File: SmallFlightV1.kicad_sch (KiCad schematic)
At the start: 0 parts

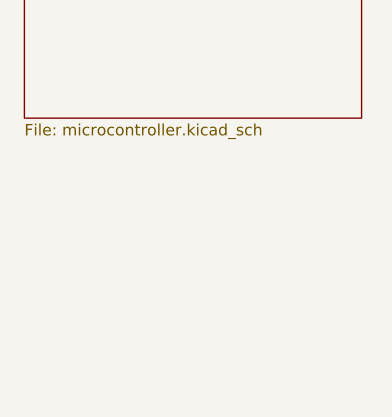
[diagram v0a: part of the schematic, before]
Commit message: more boilerplate for stm. and also power supply using LDO and USB
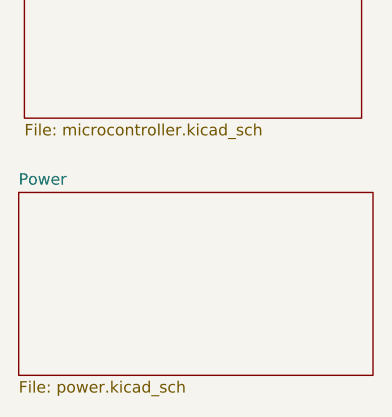
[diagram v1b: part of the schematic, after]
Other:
- added sheet Power (power.kicad_sch)
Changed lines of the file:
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@@
+		)
+	)
+	(sheet
+		(at 125.095 71.755)
+		(size 39.37 20.32)
+		(exclude_from_sim no)
+		(in_bom yes)
+		(on_board yes)
+		(dnp no)
+		(fields_autoplaced yes)
+		(stroke
+			(width 0.1524)
+			(type solid)
+		)
+		(fill
+			(color 0 0 0 0.0000)
+		)
+		(property "Sheetname" "Power"
+			(at 125.095 71.0434 0)
+			(effects
+				(font
+					(size 1.27 1.27)
+				)
+				(justify left bottom)
+			)
+		)
+		(property "Sheetfile" "power.kicad_sch"
+			(at 125.095 92.6596 0)
+			(effects
+				(font
+					(size 1.27 1.27)
+				)
+				(justify left top)
+			)
+		)
+		(instances
+			(project "SmallFlightV1"
+				(path "/5a8b04a1-a6d6-48bd-ac5f-d4986cb92d03"
+					(page "3")
+				)
+			)
 		)
 	)

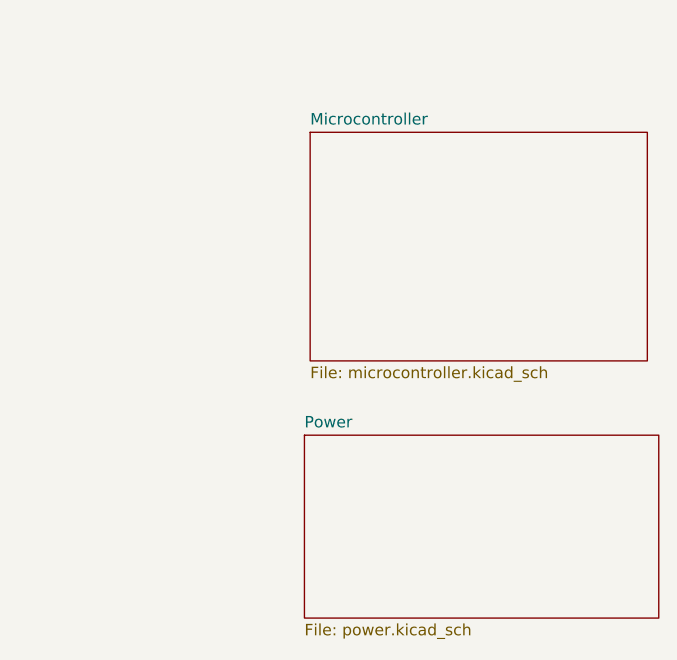
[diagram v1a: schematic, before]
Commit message: base mcu decoupling cap routing
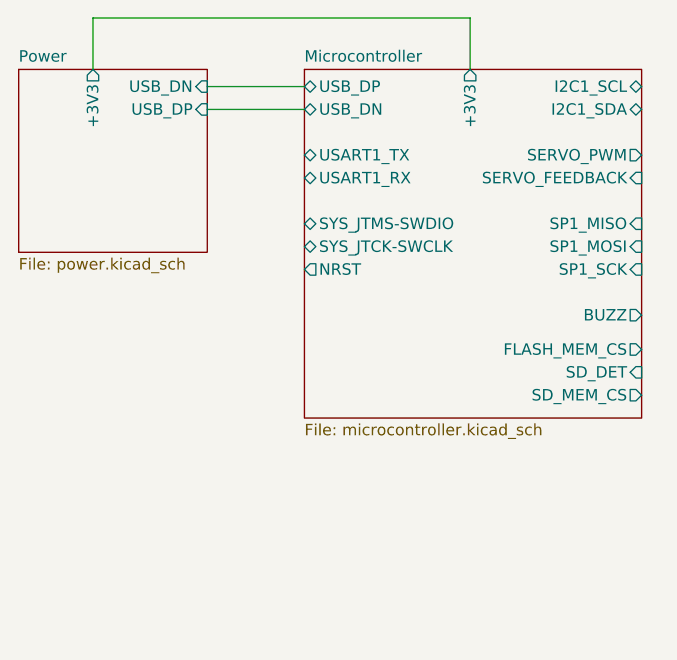
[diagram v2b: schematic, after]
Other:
- sheet Microcontroller ports: added +3V3, BUZZ, FLASH_MEM_CS, I2C1_SCL, I2C1_SDA, NRST, SD_DET, SD_MEM_CS, SERVO_FEEDBACK, SERVO_PWM, SP1_MISO, SP1_MOSI, SP1_SCK, SYS_JTCK-SWCLK, SYS_JTMS-SWDIO, USART1_RX, USART1_TX, USB_DN, USB_DP; removed none
- sheet Power ports: added +3V3, USB_DN, USB_DP; removed none
